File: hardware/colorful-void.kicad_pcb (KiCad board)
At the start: 2 copper layers, 26.7 x 24.4 mm, 7 parts, among them J1 Raspberry_Pi_Zero, J2 Conn_01x02, J3 Conn_01x03, U1 74AHCT125

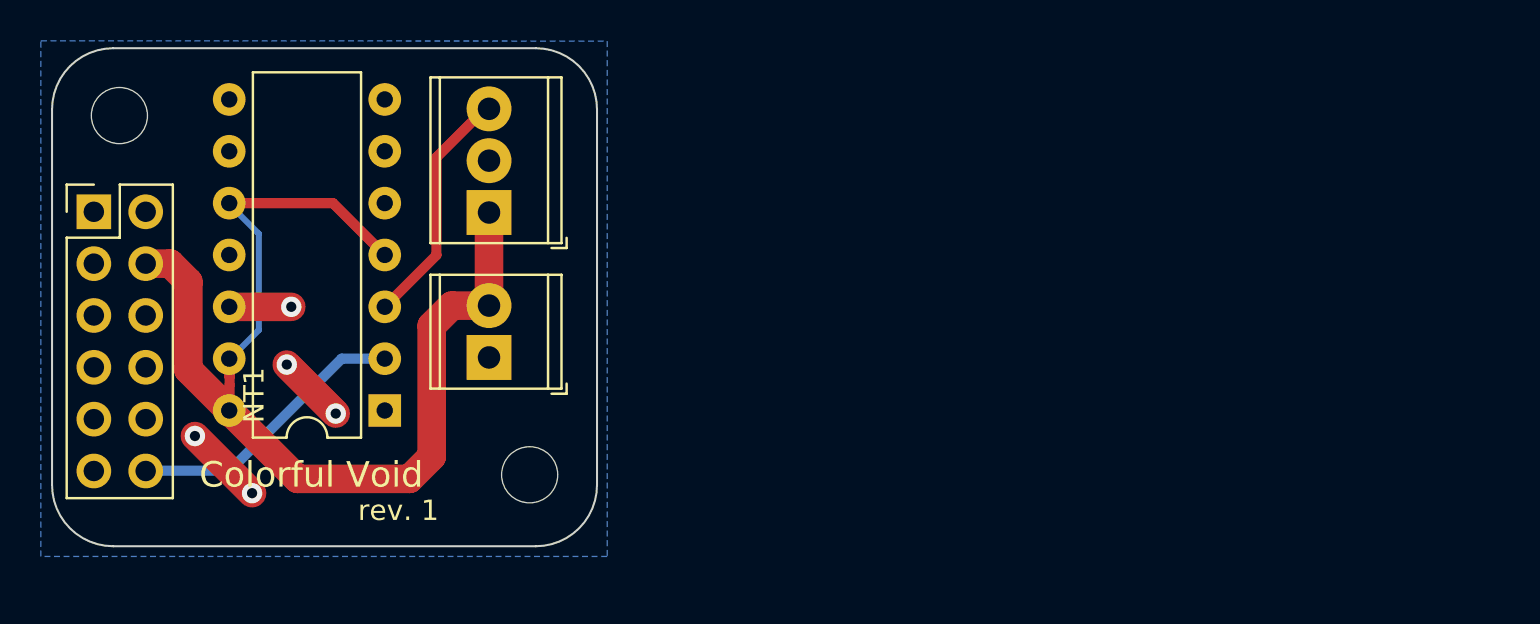
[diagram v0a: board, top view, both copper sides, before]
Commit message: Current limiting resistor on LED data line
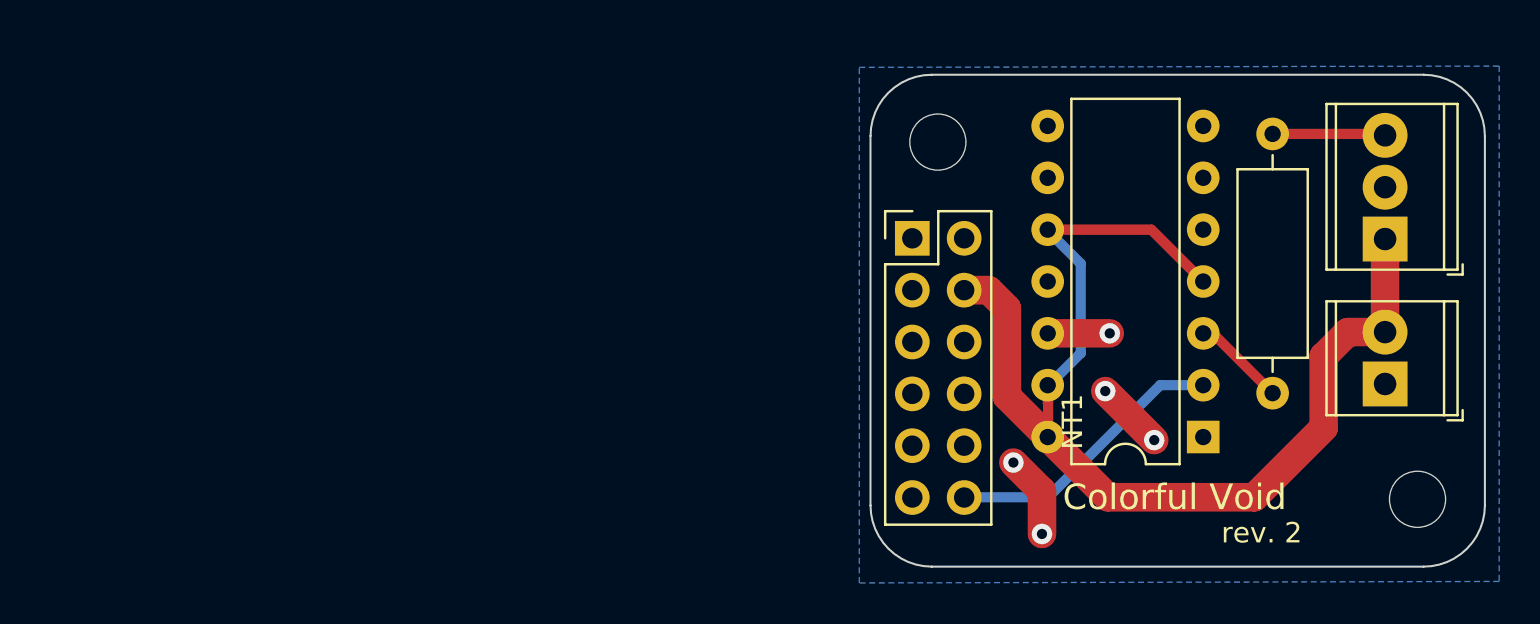
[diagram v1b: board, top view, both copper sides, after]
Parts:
- added R1: 470, Resistor_THT:R_Axial_DIN0309_L9.0mm_D3.2mm_P12.70mm_Horizontal, F.Cu at (162.1, 91.8)
- moved J2 43.9 mm to (167.9, 105.3)
- moved J3 43.9 mm to (167.9, 96.9)
- moved H1 43.5 mm to (169.2, 109.7)
- moved J1 40.1 mm to (144.4, 96.9)
- moved H2 40.1 mm to (145.7, 92.2)
- moved NT1 40.1 mm to (151.1, 105.9)
- moved U1 40.1 mm to (158.7, 106.7)
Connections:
- U1 pad 3: LED_D -> Net-(R1-Pad2)
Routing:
- net LED_D: track 11.9 -> 5.54 mm
- net Net-(R1-Pad2): track 0.00 -> 4.61 mm
- net LED_VCC: track 35.5 -> 37.3 mm
- net LED_GND: track 11.2 -> 10.5 mm
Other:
- board size 26.7 x 24.4 mm -> 30.1 x 24.1 mm
- board text added: "rev. 2"
- board text removed: "rev. 1"

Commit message: Minor PCB routing optimization
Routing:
- net LED_GND: track 10.5 -> 0.00 mm, vias 5 -> 0
- net LED_VCC: track 37.3 -> 36.1 mm
- net LED_CTRL: vias 0 -> 2
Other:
- board text added: "rev. 2.1"
- board text removed: "rev. 2"
